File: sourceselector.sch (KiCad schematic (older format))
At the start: 35 parts, among them J14 RCAJack, J15 RCAJack, J16 XLR4BODYPIN, J17 XLR4BODYPIN, J18 RCAJack, J19 RCAJack, J20 RCAJack, J21 RCAJack, SW2 SW_SPST, SW3 SW_SPST, U10 THAT1200, U11 THAT1200

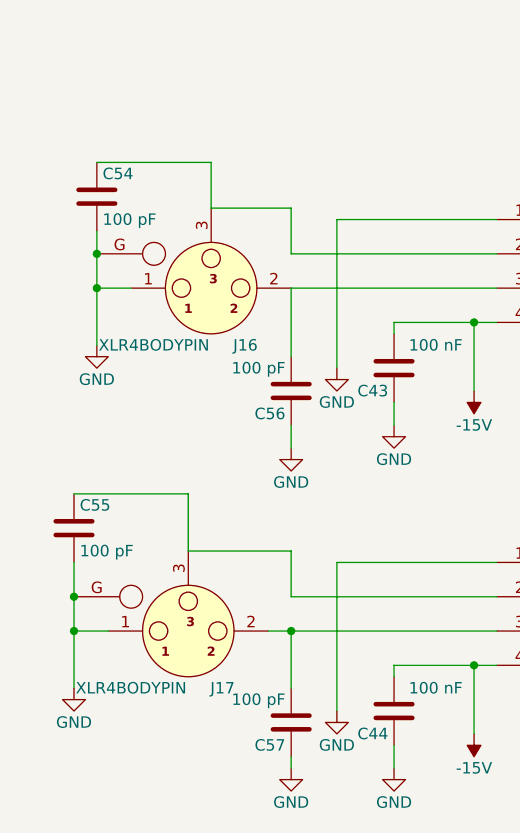
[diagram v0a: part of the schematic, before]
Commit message: Added jumpers to connect shields of XLR to ground
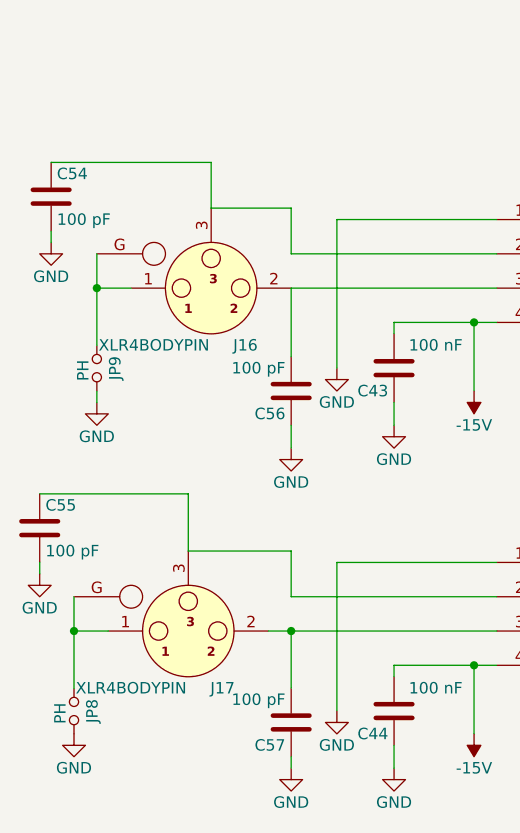
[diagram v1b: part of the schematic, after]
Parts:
- added JP8, JP9: PH, Pin_Headers:Pin_Header_Straight_1x02_Pitch2.54mm, symbol Jumper_NO_Small
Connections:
- net GND: now also JP8.2, JP9.2; no longer J16.1, J16.G, J17.1, J17.G
- new net: J16.1, J16.G, JP9.1
- new net: J17.1, J17.G, JP8.1
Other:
- moved on the sheet: C54, C55
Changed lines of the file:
@@
 $EndComp
 $Comp
-L GND #PWR74
+L GND #PWR76
 U 1 1 60561D15
 P 6250 2400
-F 0 "#PWR74" H 6250 2150 50  0001 C CNN
+F 0 "#PWR76" H 6250 2150 50  0001 C CNN
 F 1 "GND" H 6250 2250 50  0000 C CNN
 F 2 "" H 6250 2400 50  0001 C CNN
@@
 $EndComp
 $Comp
-L GND #PWR75
+L GND #PWR77
 U 1 1 60562B29
 P 6250 3750
-F 0 "#PWR75" H 6250 3500 50  0001 C CNN
+F 0 "#PWR77" H 6250 3500 50  0001 C CNN
 F 1 "GND" H 6250 3600 50  0000 C CNN
 F 2 "" H 6250 3750 50  0001 C CNN
@@
 $EndComp
 $Comp
-L GND #PWR72
+L GND #PWR74
 U 1 1 60562CEF
 P 6100 4200
-F 0 "#PWR72" H 6100 3950 50  0001 C CNN
+F 0 "#PWR74" H 6100 3950 50  0001 C CNN
 F 1 "GND" H 6100 4050 50  0000 C CNN
 F 2 "" H 6100 4200 50  0001 C CNN
@@
 $EndComp
 $Comp
-L GND #PWR71
+L GND #PWR73
 U 1 1 60562D21
 P 6100 2850
-F 0 "#PWR71" H 6100 2600 50  0001 C CNN
+F 0 "#PWR73" H 6100 2600 50  0001 C CNN
 F 1 "GND" H 6100 2700 50  0000 C CNN
 F 2 "" H 6100 2850 50  0001 C CNN
@@
 $EndComp
 $Comp
-L GND #PWR73
+L GND #PWR75
 U 1 1 60562EBA
 P 6200 5500
-F 0 "#PWR73" H 6200 5250 50  0001 C CNN
+F 0 "#PWR75" H 6200 5250 50  0001 C CNN
 F 1 "GND" H 6200 5350 50  0000 C CNN
 F 2 "" H 6200 5500 50  0001 C CNN
@@
 $EndComp
 $Comp
-L GND #PWR70
+L GND #PWR72
 U 1 1 60562EF9
 P 6050 5950
-F 0 "#PWR70" H 6050 5700 50  0001 C CNN
+F 0 "#PWR72" H 6050 5700 50  0001 C CNN
 F 1 "GND" H 6050 5800 50  0000 C CNN
 F 2 "" H 6050 5950 50  0001 C CNN
@@
 $EndComp
 $Comp
-L GND #PWR76
+L GND #PWR78
 U 1 1 60563DED
 P 8200 1700
-F 0 "#PWR76" H 8200 1450 50  0001 C CNN
+F 0 "#PWR78" H 8200 1450 50  0001 C CNN
 F 1 "GND" H 8200 1550 50  0000 C CNN
 F 2 "" H 8200 1700 50  0001 C CNN
@@
 $EndComp
 $Comp
-L GND #PWR77
+L GND #PWR79
 U 1 1 60563ECE
 P 9500 4100
-F 0 "#PWR77" H 9500 3850 50  0001 C CNN
+F 0 "#PWR79" H 9500 3850 50  0001 C CNN
 F 1 "GND" H 9500 3950 50  0000 C CNN
 F 2 "" H 9500 4100 50  0001 C CNN
@@
 $EndComp
 $Comp
-L +15V #PWR66
+L +15V #PWR68
 U 1 1 60532FD8
 P 3950 3950
-F 0 "#PWR66" H 3950 3800 50  0001 C CNN
+F 0 "#PWR68" H 3950 3800 50  0001 C CNN
 F 1 "+15V" H 3950 4090 50  0000 C CNN
 F 2 "" H 3950 3950 50  0001 C CNN
@@
 $EndComp
 $Comp
-L -15V #PWR64
+L -15V #PWR66
 U 1 1 60533183
 P 2450 5000
-F 0 "#PWR64" H 2450 5100 50  0001 C CNN
+F 0 "#PWR66" H 2450 5100 50  0001 C CNN
 F 1 "-15V" H 2450 5150 50  0000 C CNN
 F 2 "" H 2450 5000 50  0001 C CNN
@@
 $EndComp
 $Comp
-L GND #PWR62
+L GND #PWR64
 U 1 1 605335B4
 P 2100 5150
-F 0 "#PWR62" H 2100 4900 50  0001 C CNN
+F 0 "#PWR64" H 2100 4900 50  0001 C CNN
 F 1 "GND" H 2100 5000 50  0000 C CNN
 F 2 "" H 2100 5150 50  0001 C CNN
@@
 $EndComp
 $Comp
-L GND #PWR68
+L GND #PWR70
 U 1 1 60534F36
 P 4300 4800
-F 0 "#PWR68" H 4300 4550 50  0001 C CNN
+F 0 "#PWR70" H 4300 4550 50  0001 C CNN
 F 1 "GND" H 4300 4650 50  0000 C CNN
 F 2 "" H 4300 4800 50  0001 C CNN
@@
 $EndComp
 $Comp
-L GND #PWR60
+L GND #PWR62
 U 1 1 6053532B
 P 1850 4900
-F 0 "#PWR60" H 1850 4650 50  0001 C CNN
+F 0 "#PWR62" H 1850 4650 50  0001 C CNN
 F 1 "GND" H 1850 4750 50  0000 C CNN
 F 2 "" H 1850 4900 50  0001 C CNN
@@
 $EndComp
 $Comp
-L GND #PWR57
+L GND #PWR59
 U 1 1 605357E5
-P 800 4800
-F 0 "#PWR57" H 800 4550 50  0001 C CNN
-F 1 "GND" H 800 4650 50  0000 C CNN
-F 2 "" H 800 4800 50  0001 C CNN
-F 3 "" H 800 4800 50  0001 C CNN
-	1    800  4800
+P 800 5050
+F 0 "#PWR59" H 800 4800 50  0001 C CNN
+F 1 "GND" H 800 4900 50  0000 C CNN
+F 2 "" H 800 5050 50  0001 C CNN
+F 3 "" H 800 5050 50  0001 C CNN
+	1    800  5050
 	1    0    0    -1
 $EndComp
@@
 $EndComp
 $Comp
-L +15V #PWR67
+L +15V #PWR69
 U 1 1 60535F34
 P 3950 5450
-F 0 "#PWR67" H 3950 5300 50  0001 C CNN
+F 0 "#PWR69" H 3950 5300 50  0001 C CNN
 F 1 "+15V" H 3950 5590 50  0000 C CNN
 F 2 "" H 3950 5450 50  0001 C CNN
@@
 $EndComp
 $Comp
-L -15V #PWR65
+L -15V #PWR67
 U 1 1 60535F3C
 P 2450 6500
-F 0 "#PWR65" H 2450 6600 50  0001 C CNN
+F 0 "#PWR67" H 2450 6600 50  0001 C CNN
 F 1 "-15V" H 2450 6650 50  0000 C CNN
 F 2 "" H 2450 6500 50  0001 C CNN
@@
 $EndComp
 $Comp
-L GND #PWR63
+L GND #PWR65
 U 1 1 60535F4A
 P 2100 6650
-F 0 "#PWR63" H 2100 6400 50  0001 C CNN
+F 0 "#PWR65" H 2100 6400 50  0001 C CNN
 F 1 "GND" H 2100 6500 50  0000 C CNN
 F 2 "" H 2100 6650 50  0001 C CNN
@@
 $EndComp
 $Comp
-L GND #PWR69
+L GND #PWR71
 U 1 1 60535F71
 P 4300 6300
-F 0 "#PWR69" H 4300 6050 50  0001 C CNN
+F 0 "#PWR71" H 4300 6050 50  0001 C CNN
 F 1 "GND" H 4300 6150 50  0000 C CNN
 F 2 "" H 4300 6300 50  0001 C CNN
@@
 $EndComp
 $Comp
-L GND #PWR61
+L GND #PWR63
 U 1 1 60535F7D
 P 1850 6400
-F 0 "#PWR61" H 1850 6150 50  0001 C CNN
+F 0 "#PWR63" H 1850 6150 50  0001 C CNN
 F 1 "GND" H 1850 6250 50  0000 C CNN
 F 2 "" H 1850 6400 50  0001 C CNN
@@
 $EndComp
 $Comp
-L GND #PWR56
+L GND #PWR58
 U 1 1 60535F87
-P 700 6300
-F 0 "#PWR56" H 700 6050 50  0001 C CNN
-F 1 "GND" H 700 6150 50  0000 C CNN
-F 2 "" H 700 6300 50  0001 C CNN
-F 3 "" H 700 6300 50  0001 C CNN
-	1    700  6300
+P 700 6500
+F 0 "#PWR58" H 700 6250 50  0001 C CNN
+F 1 "GND" H 700 6350 50  0000 C CNN
+F 2 "" H 700 6500 50  0001 C CNN
+F 3 "" H 700 6500 50  0001 C CNN
+	1    700  6500
 	1    0    0    -1
 $EndComp
@@
 L C C54
 U 1 1 605414C0
-P 800 4150
-F 0 "C54" H 825 4250 50  0000 L CNN
-F 1 "100 pF" H 825 4050 50  0000 L CNN
-F 2 "Capacitors_THT:C_Disc_D5.0mm_W2.5mm_P5.00mm" H 838 4000 50  0001 C CIB
-F 3 "" H 800 4150 50  0001 C CNN
-	1    800  4150
+P 600 4150
+F 0 "C54" H 625 4250 50  0000 L CNN
+F 1 "100 pF" H 625 4050 50  0000 L CNN
+F 2 "Capacitors_THT:C_Disc_D5.0mm_W2.5mm_P5.00mm" H 638 4000 50  0001 C CIB
+F 3 "" H 600 4150 50  0001 C CNN
+	1    600  4150
 	1    0    0    -1
 $EndComp
@@
 $EndComp
 $Comp
-L GND #PWR58
+L GND #PWR60
 U 1 1 60541DBA
 P 1650 5250
-F 0 "#PWR58" H 1650 5000 50  0001 C CNN
+F 0 "#PWR60" H 1650 5000 50  0001 C CNN
 F 1 "GND" H 1650 5100 50  0000 C CNN
 F 2 "" H 1650 5250 50  0001 C CNN
@@
 L C C55
 U 1 1 60542053
-P 700 5600
-F 0 "C55" H 725 5700 50  0000 L CNN
-F 1 "100 pF" H 725 5500 50  0000 L CNN
-F 2 "Capacitors_THT:C_Disc_D5.0mm_W2.5mm_P5.00mm" H 738 5450 50  0001 C CIB
-F 3 "" H 700 5600 50  0001 C CNN
-	1    700  5600
+P 550 5600
+F 0 "C55" H 575 5700 50  0000 L CNN
+F 1 "100 pF" H 575 5500 50  0000 L CNN
+F 2 "Capacitors_THT:C_Disc_D5.0mm_W2.5mm_P5.00mm" H 588 5450 50  0001 C CIB
+F 3 "" H 550 5600 50  0001 C CNN
+	1    550  5600
 	1    0    0    -1
 $EndComp
@@
 $EndComp
 $Comp
-L GND #PWR59
+L GND #PWR61
 U 1 1 60543114
 P 1650 6650
-F 0 "#PWR59" H 1650 6400 50  0001 C CNN
+F 0 "#PWR61" H 1650 6400 50  0001 C CNN
 F 1 "GND" H 1650 6500 50  0000 C CNN
 F 2 "" H 1650 6650 50  0001 C CNN
@@
 	1300 4200 1300 4000
 Wire Wire Line
-	1300 4000 800  4000
-Connection ~ 800  4400
+	1300 4000 600  4000
 Connection ~ 800  4550
 Wire Wire Line
-	800  4300 800  4800
-Wire Wire Line
-	1200 5450 700  5450
+	800  4400 800  4800
+Wire Wire Line
+	550  5450 1200 5450
 Wire Wire Line
 	1650 5700 1200 5700
@@
 Wire Wire Line
 	700  6050 850  6050
-Connection ~ 700  5900
-Wire Wire Line
-	700  5750 700  6300
+Wire Wire Line
+	700  5900 700  6300
 Wire Wire Line
 	1200 5700 1200 5450
@@
 	5100 6250 5100 5300
 $Comp
-L -15V #PWR79
+L -15V #PWR81
 U 1 1 60700AF7
 P 10850 3950
-F 0 "#PWR79" H 10850 4050 50  0001 C CNN
+F 0 "#PWR81" H 10850 4050 50  0001 C CNN
 F 1 "-15V" H 10850 4100 50  0000 C CNN
 F 2 "" H 10850 3950 50  0001 C CNN
@@
 $EndComp
 $Comp
-L -15V #PWR78
+L -15V #PWR80
 U 1 1 607197DB
 P 9800 1700
-F 0 "#PWR78" H 9800 1800 50  0001 C CNN
+F 0 "#PWR80" H 9800 1800 50  0001 C CNN
 F 1 "-15V" H 9800 1850 50  0000 C CNN
 F 2 "" H 9800 1700 50  0001 C CNN
@@
 Wire Wire Line
 	9800 1700 9800 1600
+$Comp
+L Jumper_NO_Small JP9
+U 1 1 608F780E
+P 800 4900
+F 0 "JP9" H 800 4980 50  0000 C CNN
+F 1 "PH" H 810 4840 50  0000 C CNN
+F 2 "Pin_Headers:Pin_Header_Straight_1x02_Pitch2.54mm" H 800 4900 50  0001 C CNN
+F 3 "" H 800 4900 50  0001 C CNN
+	1    800  4900
+	0    1    1    0
+$EndComp
+Wire Wire Line
+	800  5000 800  5050
+$Comp
+L Jumper_NO_Small JP8
+U 1 1 608F7A77
+P 700 6400
+F 0 "JP8" H 700 6480 50  0000 C CNN
+F 1 "PH" H 710 6340 50  0000 C CNN
+F 2 "Pin_Headers:Pin_Header_Straight_1x02_Pitch2.54mm" H 700 6400 50  0001 C CNN
+F 3 "" H 700 6400 50  0001 C CNN
+	1    700  6400
+	0    1    1    0
+$EndComp
+$Comp
+L GND #PWR57
+U 1 1 608F84E9
+P 600 4350
+F 0 "#PWR57" H 600 4100 50  0001 C CNN
+F 1 "GND" H 600 4200 50  0000 C CNN
+F 2 "" H 600 4350 50  0001 C CNN
+F 3 "" H 600 4350 50  0001 C CNN
+	1    600  4350
+	1    0    0    -1
+$EndComp
+Wire Wire Line
+	600  4350 600  4300
+$Comp
+L GND #PWR56
+U 1 1 608F88DF
+P 550 5800
+F 0 "#PWR56" H 550 5550 50  0001 C CNN
+F 1 "GND" H 550 5650 50  0000 C CNN
+F 2 "" H 550 5800 50  0001 C CNN
+F 3 "" H 550 5800 50  0001 C CNN
+	1    550  5800
+	1    0    0    -1
+$EndComp
+Wire Wire Line
+	550  5750 550  5800
 $EndSCHEMATC
